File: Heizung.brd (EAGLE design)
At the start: 100 x 80 mm, 41 parts, among them IC1 MEGA8-PTQFP, Q2 2N7002, Q3 2N7002

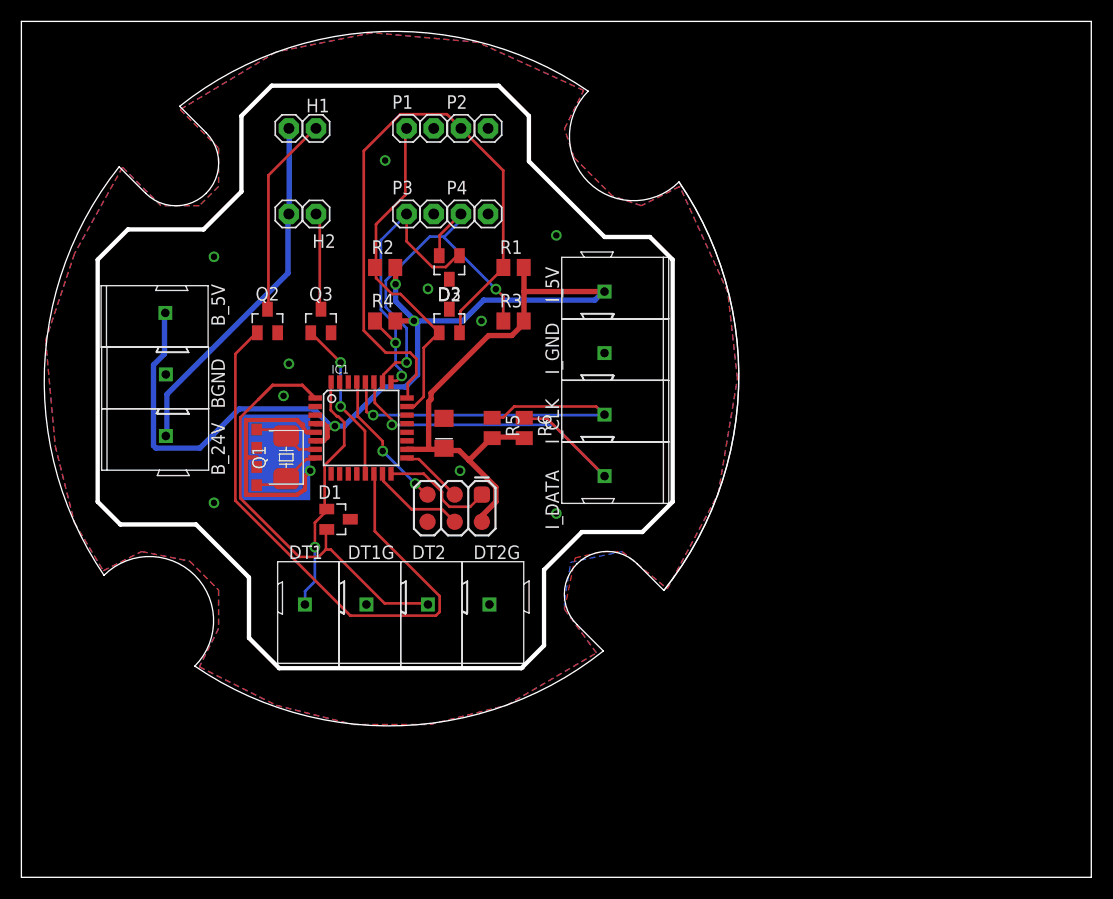
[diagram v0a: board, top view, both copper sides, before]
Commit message: additional ground on power side, outline fixed
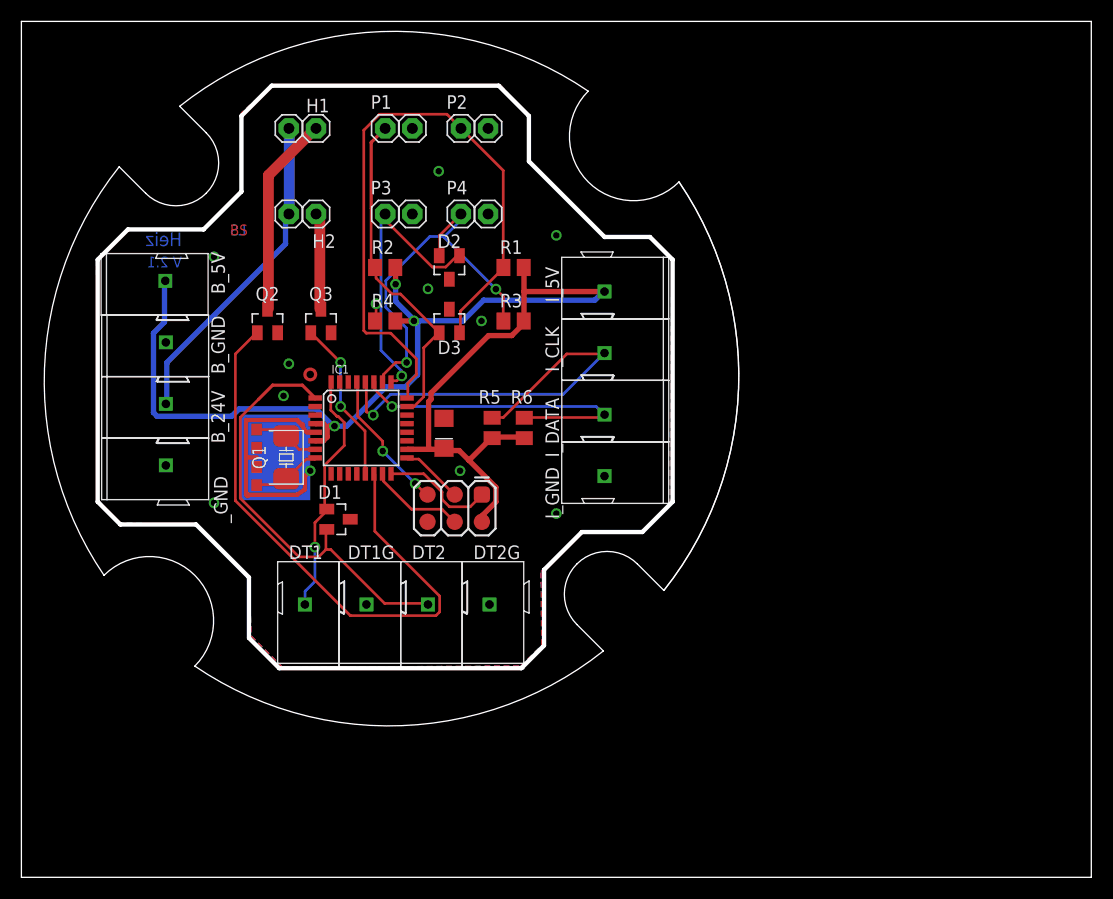
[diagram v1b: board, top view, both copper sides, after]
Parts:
- removed BGND: WAGO_243, common:WAGO_243
- added B_GND, _GND: WAGO_243, common:WAGO_243
- moved I_GND 11.5 mm to (54.5, 37.5)
- moved I_CLK 5.75 mm to (54.5, 49.0)
- moved I_DATA 5.75 mm to (54.5, 43.2)
- moved B_24V 3.00 mm to (13.5, 44.2)
- moved B_5V 3.00 mm to (13.4, 55.8)
- moved P1 2.00 mm to (34.0, 70.0)
- moved P1G 2.00 mm to (36.5, 70.0)
- moved P3 2.00 mm to (34.0, 62.0)
- moved P3G 2.00 mm to (36.5, 62.0)
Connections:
- net GND: now also B_GND.P$1, _GND.P$1; no longer BGND.P$1
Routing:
- net N$10: track 36.4 -> 30.8 mm
- net N$18: track 36.6 -> 40.8 mm
- net N$1: track 33.6 -> 30.5 mm
- net 5V: track 126.9 -> 125.5 mm
- net B2: track 60.4 -> 61.5 mm
- net B3: track 30.0 -> 29.3 mm
- net B1: track 31.9 -> 31.4 mm
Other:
- board text added: "BS"
- board text added: "Heiz"
- board text added: "LS"
- board text added: "V 2.1"

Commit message: Update auf 2.4
2-Draht-Klemmen verwendet und gedreht
Wagoklemmen nach innen gedreht
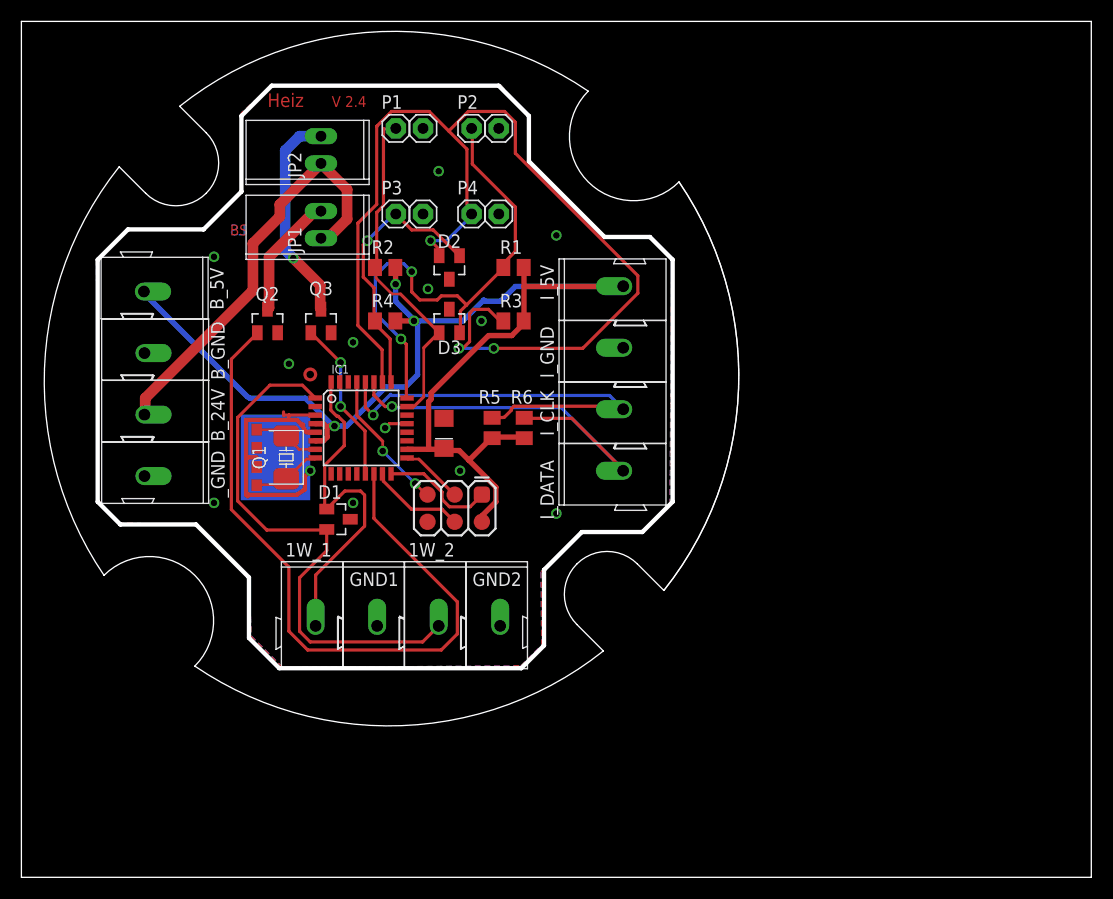
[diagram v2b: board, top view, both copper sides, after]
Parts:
- removed DT1, DT1G, DT2, DT2G: WAGO_243, common:WAGO_243
- removed H1, H1V, H2, H2V: WAGO_243, common:1X01
- added 1W_1, 1W_2, GND1, GND2: WAGO_243, common:WAGO_243
- added JP1, JP2: (no value), common:1X02_GN
- moved I_GND 12.1 mm to (56.2, 49.5), turned to 180 degrees
- moved I_CLK 5.53 mm to (56.2, 43.8), turned to 180 degrees
- moved I_DATA 5.53 mm to (56.2, 38.0), turned to 180 degrees
- moved B_24V 2.24 mm to (11.5, 43.2), turned to 0 degrees
- moved B_5V 2.24 mm to (11.4, 54.8), turned to 0 degrees
- moved B_GND 2.24 mm to (11.5, 49.0), turned to 0 degrees
- moved _GND 2.24 mm to (11.5, 37.5), turned to 0 degrees
- moved I_5V 1.82 mm to (56.2, 55.2), turned to 180 degrees
- moved P1 1.00 mm to (35.0, 70.0)
- moved P1G 1.00 mm to (37.5, 70.0)
- moved P2 1.00 mm to (42.1, 70.0)
- moved P2G 1.00 mm to (44.6, 70.0)
- moved P3 1.00 mm to (35.0, 62.0)
- moved P3G 1.00 mm to (37.5, 62.0)
- moved P4 1.00 mm to (42.1, 62.0)
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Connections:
- net GND: now also GND1.P$1, GND2.P$1; no longer DT1G.P$1, DT2G.P$1
- net N$1: now also JP1.1, JP2.1; no longer H1V.1, H2V.1
- net N$19: now also JP1.2; no longer H1.1
- net N$33: now also JP2.2; no longer H2.1
- net N$5: now also 1W_1.P$1; no longer DT1.P$1
- net N$8: now also 1W_2.P$1; no longer DT2.P$1
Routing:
- net B4: track 36.7 -> 103.8 mm, vias 2 -> 3
- net B2: track 61.5 -> 47.6 mm, vias 0 -> 2
- net N$33: track 9.11 -> 20.1 mm, vias 0 -> 1
- net N$3: track 55.7 -> 66.5 mm
- net N$8: track 40.6 -> 51.0 mm
- net N$1: track 30.5 -> 39.7 mm
- net N$5: track 23.2 -> 32.0 mm, vias 1 -> 0
- net N$10: track 30.8 -> 39.0 mm
- net N$19: track 18.8 -> 11.7 mm
- net GND: track 22.8 -> 29.5 mm, vias 11 -> 13
- net 5V: track 125.5 -> 121.7 mm
- net B3: track 29.3 -> 25.8 mm, vias 2 -> 1
- net B1: track 31.4 -> 32.1 mm
- net N$18: track 40.8 -> 41.3 mm
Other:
- board text added: "V 2.4"
- board text removed: "V 2.1"

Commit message: Längere Pads für CPU
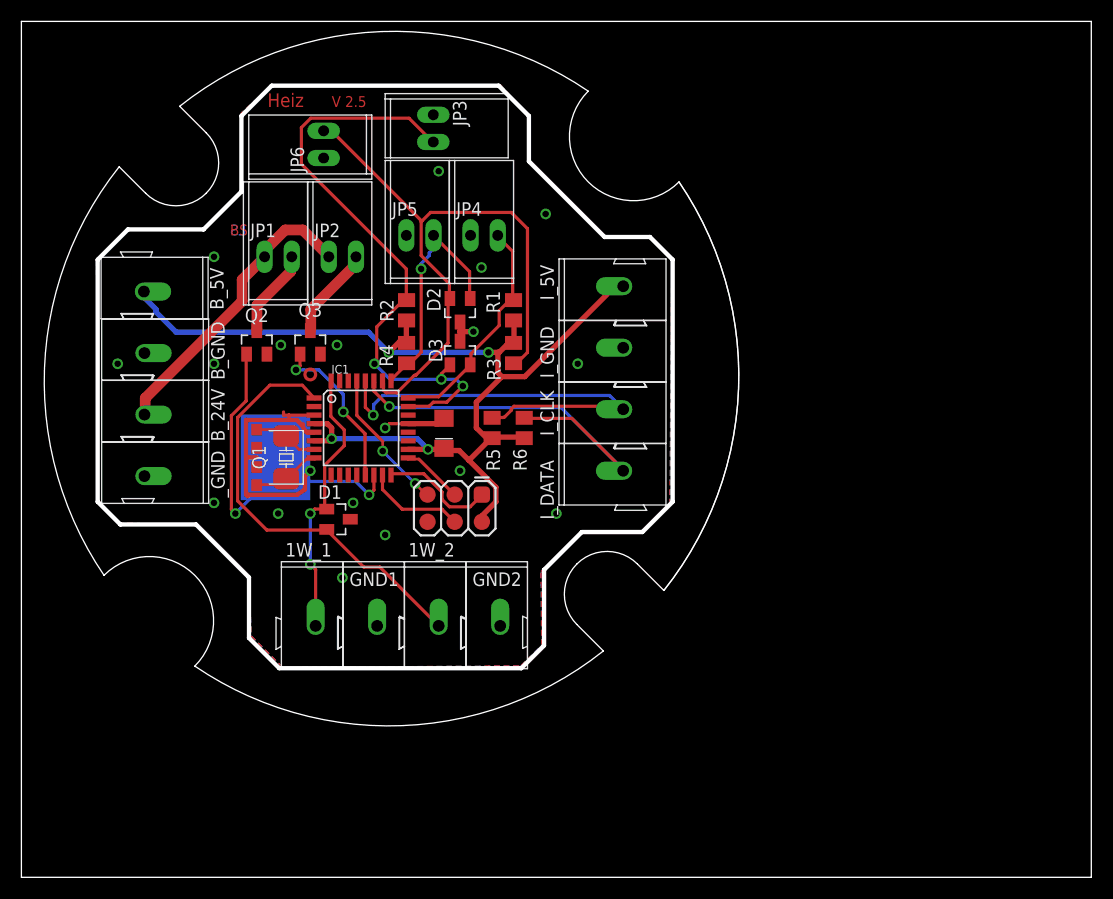
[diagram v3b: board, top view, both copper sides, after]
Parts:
- removed P1, P1G, P2, P2G, P3, P3G, P4, P4G: (no value), common:1X01
- added JP3, JP4, JP5, JP6: (no value), common:1X02_GN
- moved JP2 10.2 mm to (30.0, 58.0), turned to 0 degrees
- moved JP1 5.00 mm to (24.0, 58.0), turned to 0 degrees
- moved R2 4.47 mm to (36.0, 53.0), turned to 270 degrees
- moved D2 4.12 mm to (41.0, 53.0)
- moved R1 4.00 mm to (46.0, 53.0), turned to 270 degrees
- moved R4 3.61 mm to (36.0, 49.0), turned to 90 degrees
- moved D3 3.16 mm to (41.0, 49.0)
- moved R3 3.00 mm to (46.0, 49.0), turned to 90 degrees
- moved Q2 2.24 mm to (22.0, 50.0)
- moved Q3 2.24 mm to (27.0, 50.0)
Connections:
- net B1: now also JP3.2; no longer P1.1
- net B2: now also JP4.2; no longer P2.1
- net B3: now also JP5.2; no longer P3.1
- net B4: now also JP6.2; no longer P4.1
- net GND: now also JP3.1, JP4.1, JP5.1, JP6.1; no longer P1G.1, P2G.1, P3G.1, P4G.1
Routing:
- net B4: track 103.8 -> 58.4 mm, vias 3 -> 0
- net N$3: track 66.5 -> 32.0 mm, vias 0 -> 2
- net B1: track 32.1 -> 58.1 mm, vias 0 -> 3
- net B2: track 47.6 -> 22.0 mm, vias 2 -> 0
- net 5V: track 121.7 -> 102.6 mm, vias 3 -> 4
- net N$1: track 39.7 -> 27.9 mm
- net N$33: track 20.1 -> 8.70 mm, vias 1 -> 0
- net N$8: track 51.0 -> 40.6 mm
- net GND: track 29.5 -> 36.0 mm, vias 13 -> 19
- net N$5: track 32.0 -> 25.9 mm, vias 0 -> 2
- net N$19: track 11.7 -> 8.31 mm
- net B3: track 25.8 -> 22.9 mm
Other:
- board text added: "V 2.5"
- board text removed: "V 2.4"

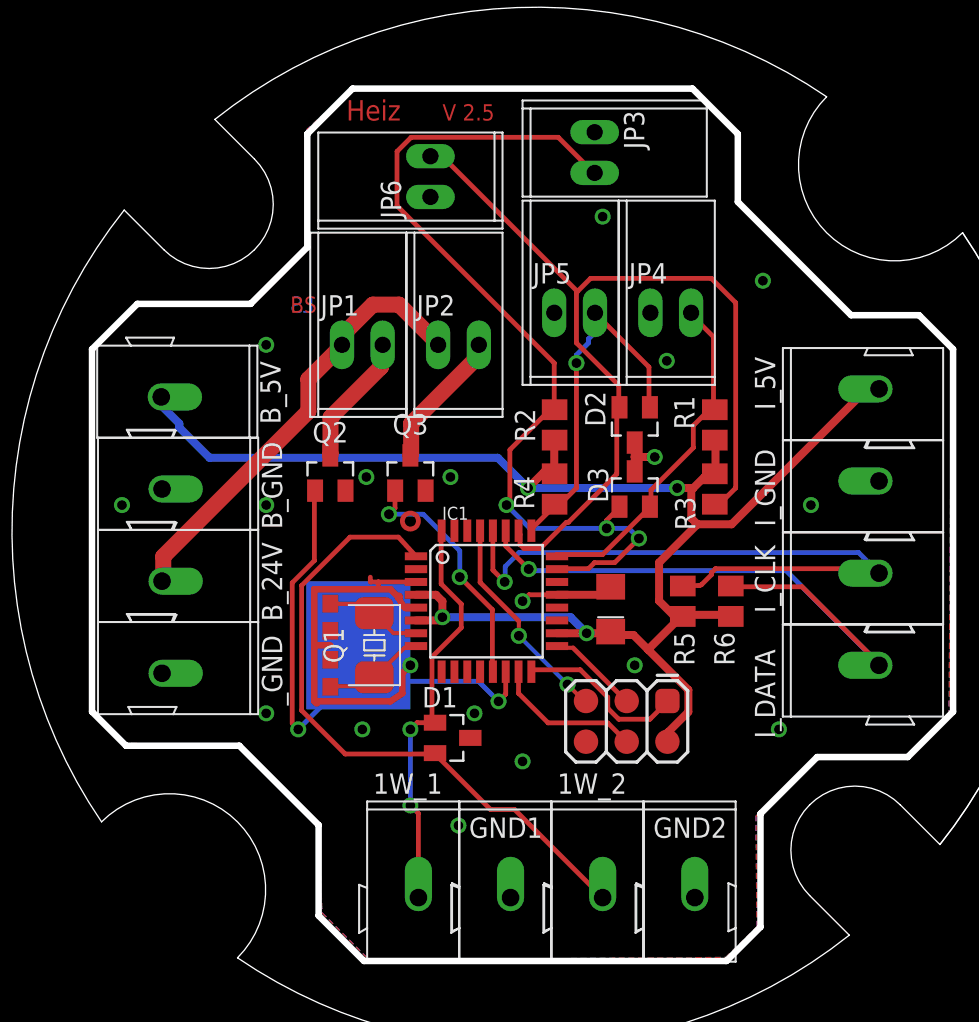
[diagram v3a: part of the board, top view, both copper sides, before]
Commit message: V2.7: add diode (for switching relays)
general clean-up
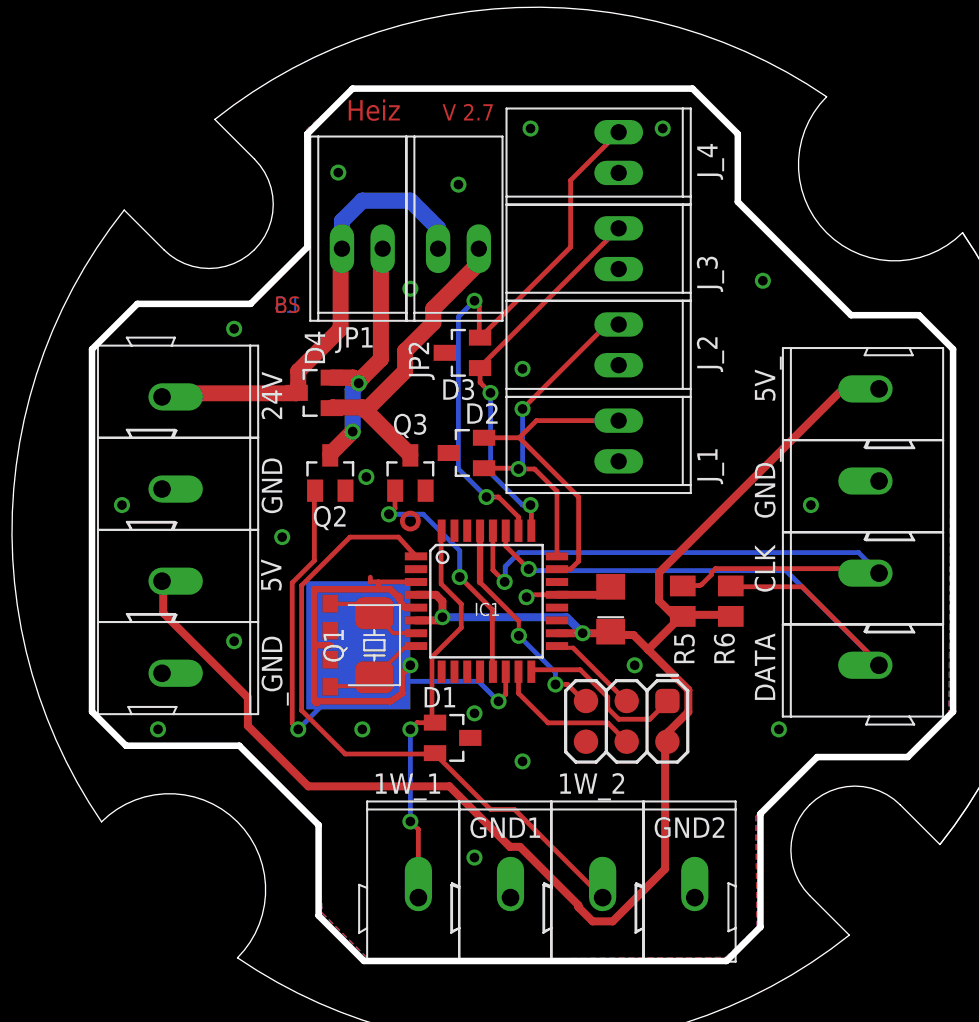
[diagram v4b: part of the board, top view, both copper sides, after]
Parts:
- removed B_5V: WAGO_243, common:WAGO_243
- removed JP3, JP4, JP5, JP6: (no value), common:1X02_GN
- removed R1, R2, R3, R4: (no value), common:M0805
- added 24V: WAGO_243, common:WAGO_243
- added D4: BAS40-05, common:SOT23
- added J_1, J_2, J_3, J_4: (no value), common:1X02_GN
- moved D3 13.7 mm to (30.2, 57.5), turned to 90 degrees
- moved D2 10.6 mm to (30.5, 51.2), turned to 90 degrees
- moved JP1 6.00 mm to (24.0, 64.0)
- moved JP2 6.00 mm to (30.0, 64.0)
- renumbered B_24V to 5V, I_5V to 5V_, I_CLK to CLK, I_DATA to DATA, I_GND to GND_
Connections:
- net 5V: now also 5V.P$1; no longer B_5V.P$1, R1.2, R2.2, R3.2, R4.2
- net B1: now also D2.2, J_1.2; no longer D3.1, JP3.2, R2.1
- net B2: now also D2.1, J_2.2; no longer D3.2, JP4.2, R1.1
- net B3: now also D3.1, J_3.2; no longer D2.1, JP5.2, R4.1
- net B4: now also D3.2, J_4.2; no longer D2.2, JP6.2, R3.1
- net GND: now also J_1.1, J_2.1, J_3.1, J_4.1; no longer JP3.1, JP4.1, JP5.1, JP6.1
- net N$1: now also 24V.P$1, D4.3; no longer 5V.P$1
- net N$19: now also D4.2
- net N$33: now also D4.1
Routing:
- net B1: track 58.1 -> 19.6 mm, vias 3 -> 0
- net B4: track 58.4 -> 35.6 mm, vias 0 -> 2
- net N$33: track 8.70 -> 19.2 mm
- net N$19: track 8.31 -> 16.0 mm, vias 0 -> 2
- net 5V: track 102.6 -> 107.3 mm, vias 4 -> 2
- net GND: track 36.0 -> 32.8 mm, vias 19 -> 22
- net B3: track 22.9 -> 24.1 mm, vias 1 -> 2
- net N$1: track 27.9 -> 28.9 mm
- net B2: track 22.0 -> 21.2 mm, vias 0 -> 2
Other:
- board text added: "GND"
- board text added: "V 2.7"
- board text removed: "V 2.5"

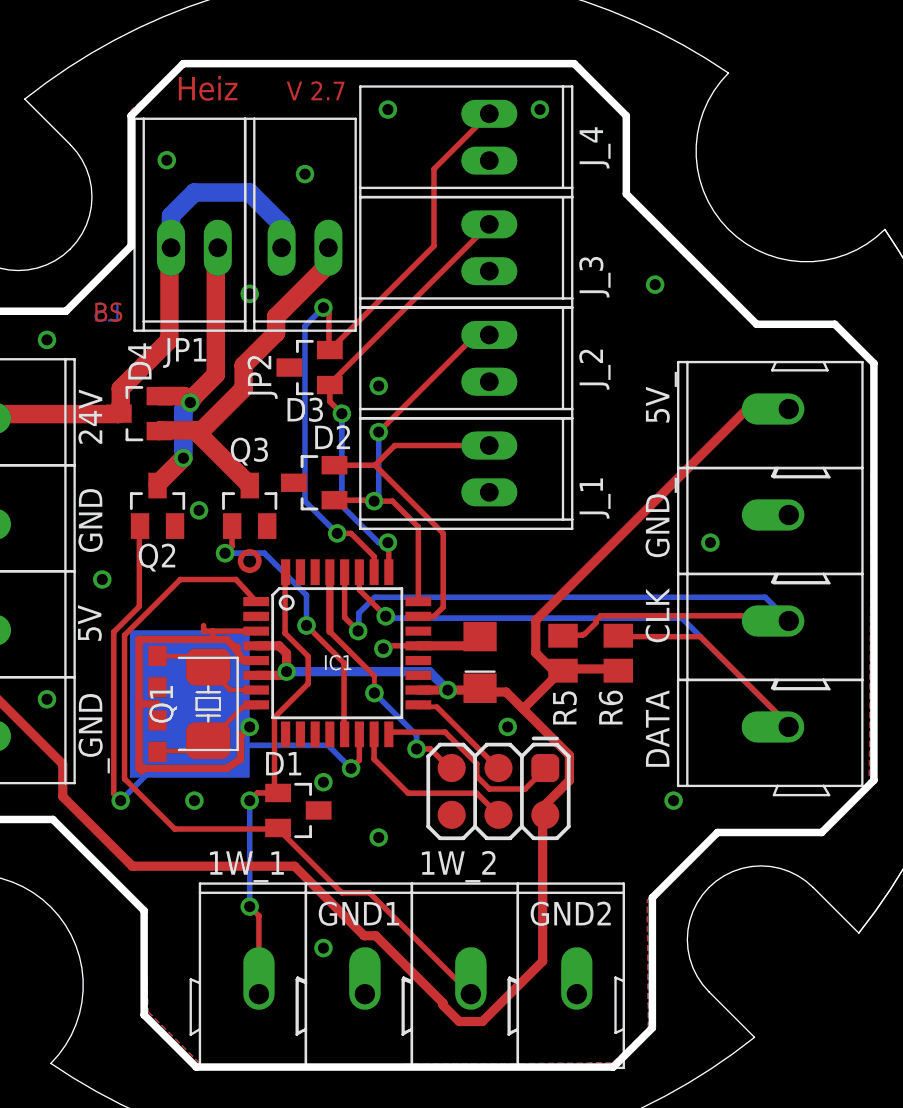
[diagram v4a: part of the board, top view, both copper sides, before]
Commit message: change min width to 3.5mm, fix XTAL
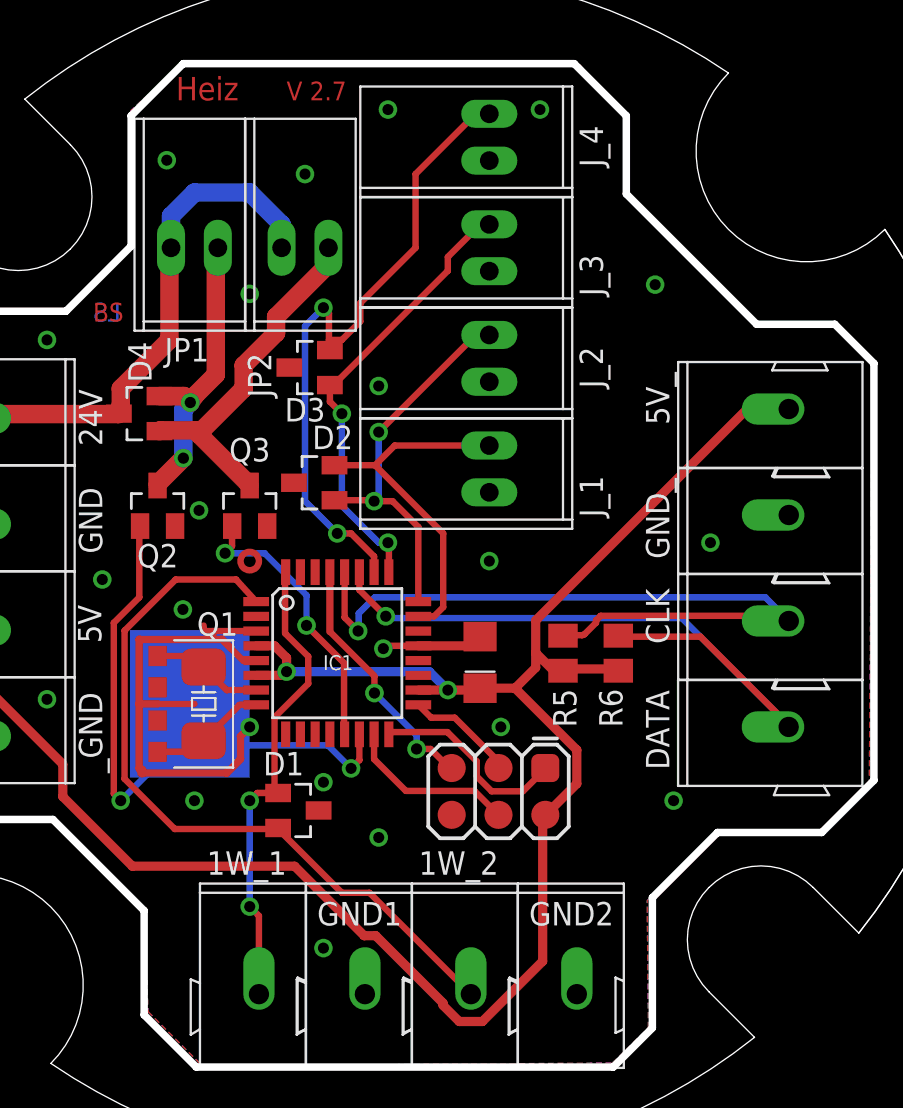
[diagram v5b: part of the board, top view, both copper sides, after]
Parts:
- moved Q1 0.25 mm to (24.5, 39.2)
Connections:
- new net N$41: J_1.1, J_2.1, J_3.1, J_4.1
- net GND: no longer J_1.1, J_2.1, J_3.1, J_4.1
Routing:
- net GND: track 32.8 -> 34.8 mm, vias 22 -> 24
